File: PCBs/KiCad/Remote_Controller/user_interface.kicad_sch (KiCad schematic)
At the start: 35 parts, among them SW301 SW_Push, SW302 SW_Push, SW303 SW_Push, SW304 SW_Push, SW305 SW_Push, SW306 SW_Push, SW307 SW_Push, SW308 SW_Push, U301 NHD-C12832A1Z-FSW-FBW-3V3

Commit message: Add Latching Power On-Off switch circuit - allows user to turn device on and off with a tactile switch
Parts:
- SW301, SW302, SW303, SW304, SW305, SW306, SW307, SW308: footprint (none) -> Button_Switch_SMD:SW_Push_1P1T_NO_CK_PTS125Sx43PSMTR
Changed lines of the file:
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@@
 			)
 		)
-		(property "Footprint" ""
+		(property "Footprint" "Button_Switch_SMD:SW_Push_1P1T_NO_CK_PTS125Sx43PSMTR"
 			(at 120.65 107.95 0)
 			(effects
@@
 			)
 		)
-		(property "Footprint" ""
+		(property "Footprint" "Button_Switch_SMD:SW_Push_1P1T_NO_CK_PTS125Sx43PSMTR"
 			(at 161.29 107.95 0)
 			(effects
@@
 			)
 		)
-		(property "Footprint" ""
+		(property "Footprint" "Button_Switch_SMD:SW_Push_1P1T_NO_CK_PTS125Sx43PSMTR"
 			(at 161.29 137.16 0)
 			(effects
@@
 			)
 		)
-		(property "Footprint" ""
+		(property "Footprint" "Button_Switch_SMD:SW_Push_1P1T_NO_CK_PTS125Sx43PSMTR"
 			(at 120.65 137.16 0)
 			(effects
@@
 			)
 		)
-		(property "Footprint" ""
+		(property "Footprint" "Button_Switch_SMD:SW_Push_1P1T_NO_CK_PTS125Sx43PSMTR"
 			(at 80.01 137.16 0)
 			(effects
@@
 			)
 		)
-		(property "Footprint" ""
+		(property "Footprint" "Button_Switch_SMD:SW_Push_1P1T_NO_CK_PTS125Sx43PSMTR"
 			(at 201.93 137.16 0)
 			(effects
@@
 			)
 		)
-		(property "Footprint" ""
+		(property "Footprint" "Button_Switch_SMD:SW_Push_1P1T_NO_CK_PTS125Sx43PSMTR"
 			(at 80.01 107.95 0)
 			(effects
@@
 			)
 		)
-		(property "Footprint" ""
+		(property "Footprint" "Button_Switch_SMD:SW_Push_1P1T_NO_CK_PTS125Sx43PSMTR"
 			(at 201.93 107.95 0)
 			(effects

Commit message: Add Joystick footprint and passed ERC
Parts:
- JS301, JS302: footprint (none) -> Thumb_joy_stick_Library:XDCR_COM-09032
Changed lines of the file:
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@@
 			)
 		)
-		(property "Footprint" ""
+		(property "Footprint" "Thumb_joy_stick_Library:XDCR_COM-09032"
 			(at 176.53 73.66 0)
 			(effects
@@
 			)
 		)
-		(property "Footprint" ""
+		(property "Footprint" "Thumb_joy_stick_Library:XDCR_COM-09032"
 			(at 236.22 73.66 0)
 			(effects

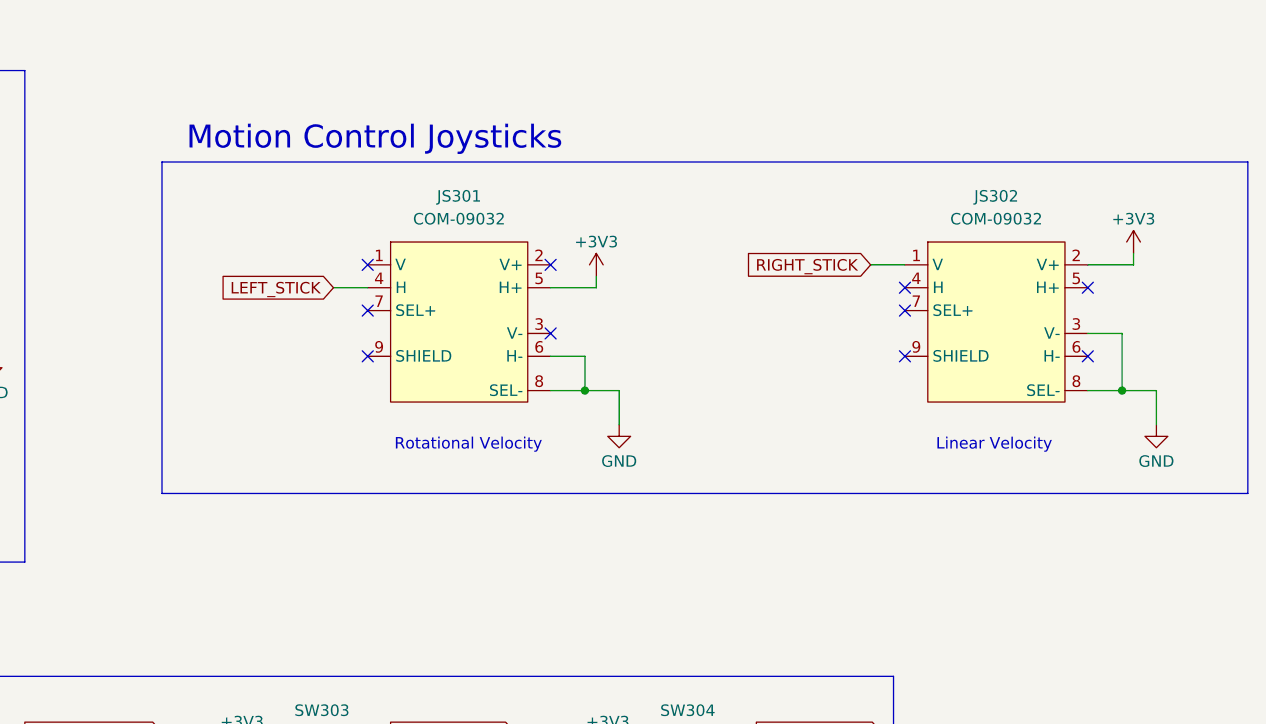
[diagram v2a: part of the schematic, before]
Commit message: Updated joystick symbol, correct Dual fet footprint and annotated news in power toggle circuit
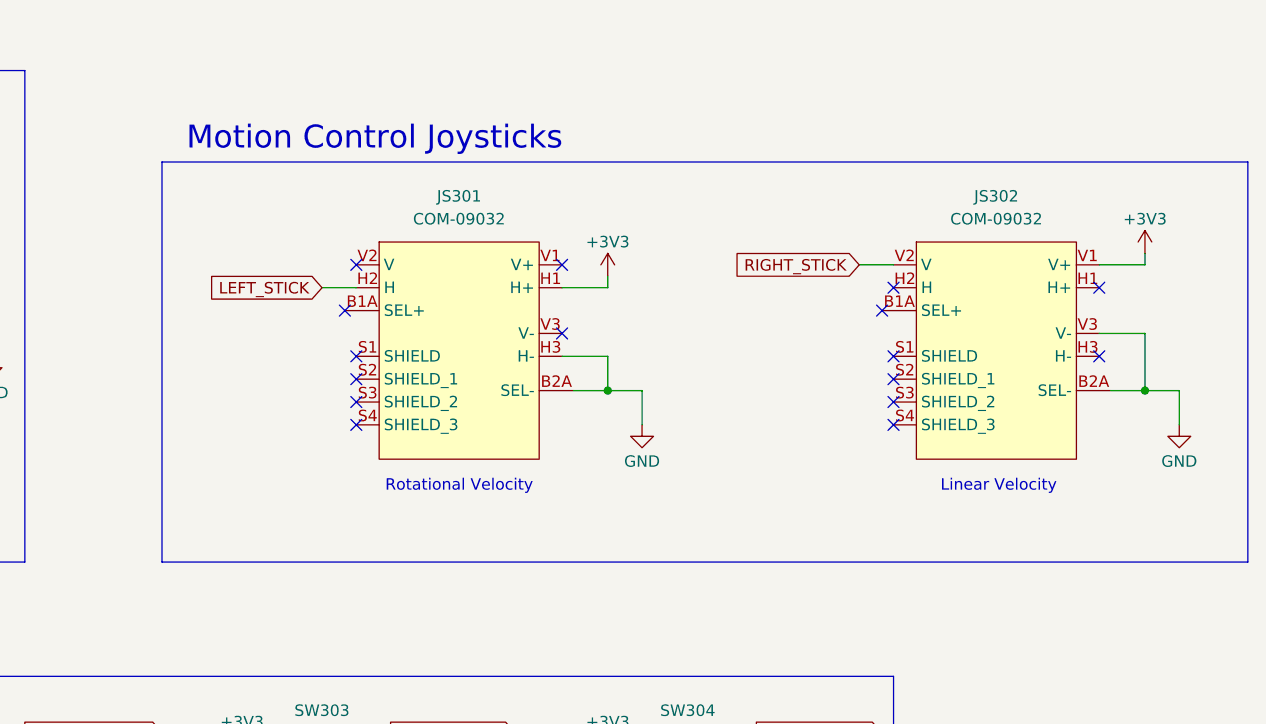
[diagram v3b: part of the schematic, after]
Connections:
- net +3V3: now also JS301.H1 (H+), JS302.V1 (V+); no longer JS301.5 (H+), JS302.2 (V+)
- net GND: now also JS301.B2A (SEL-), JS301.H3 (H-), JS302.B2A (SEL-), JS302.V3 (V-); no longer JS301.6 (H-), JS301.8 (SEL-), JS302.3 (V-), JS302.8 (SEL-)
- net LEFT_STICK: now also JS301.H2 (H); no longer JS301.4 (H)
- net RIGHT_STICK: now also JS302.V2 (V); no longer JS302.1 (V)
- no-connect marks 10 -> 16

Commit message: Added new symbol fields and completed BOM
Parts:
- C301, C307, C308: JLCPCB Part # (none) -> C72203; Manufacturer Part # (none) -> GRM155R61E225ME15D
- C302, C303, C304, C305, C306: JLCPCB Part # (none) -> C14445; Manufacturer Part # (none) -> CL05A105KP5NNNC
- C309, C310, C311, C312, C313, C314, C315, C316: JLCPCB Part # (none) -> C155422; Manufacturer Part # (none) -> CL05B104KA5NNNC
- JS301, JS302: Manufacturer Part # (none) -> COM-09032
- R301, R302, R303, R304, R305, R306, R307, R308: JLCPCB Part # (none) -> C25531; Manufacturer Part # (none) -> 0402WGJ0103TCE
- SW301, SW302, SW303, SW304, SW305, SW306, SW307, SW308: JLCPCB Part # (none) -> C455234; Manufacturer Part # (none) -> TS-1003ST-26
- U301: Manufacturer Part # (none) -> NHD-C12832A1Z-FSW-FBW-3V3

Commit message: Added silkscreen text and made manufacturing files
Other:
- title: (none) -> SurvBot - Remote Controller
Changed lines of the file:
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@@
 	(generator_version "8.0")
 	(paper "A4")
+	(title_block
+		(title "SurvBot - Remote Controller")
+		(date "2025-03-17")
+		(rev "1.0.0.")
+	)
 	(junction
 		(at 154.94 113.03)
